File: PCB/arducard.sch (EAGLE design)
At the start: 85 parts, among them J1 USB MICRO, Q1 BC817-16LT1SMD, Q2 NTR0202PL, Q3 2N7002, Q4 BSS84, Q5 2N7002, Q6 2N7002, U1 microSD, U2 ATMEGA32U4-XUAU, U3 LM3658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

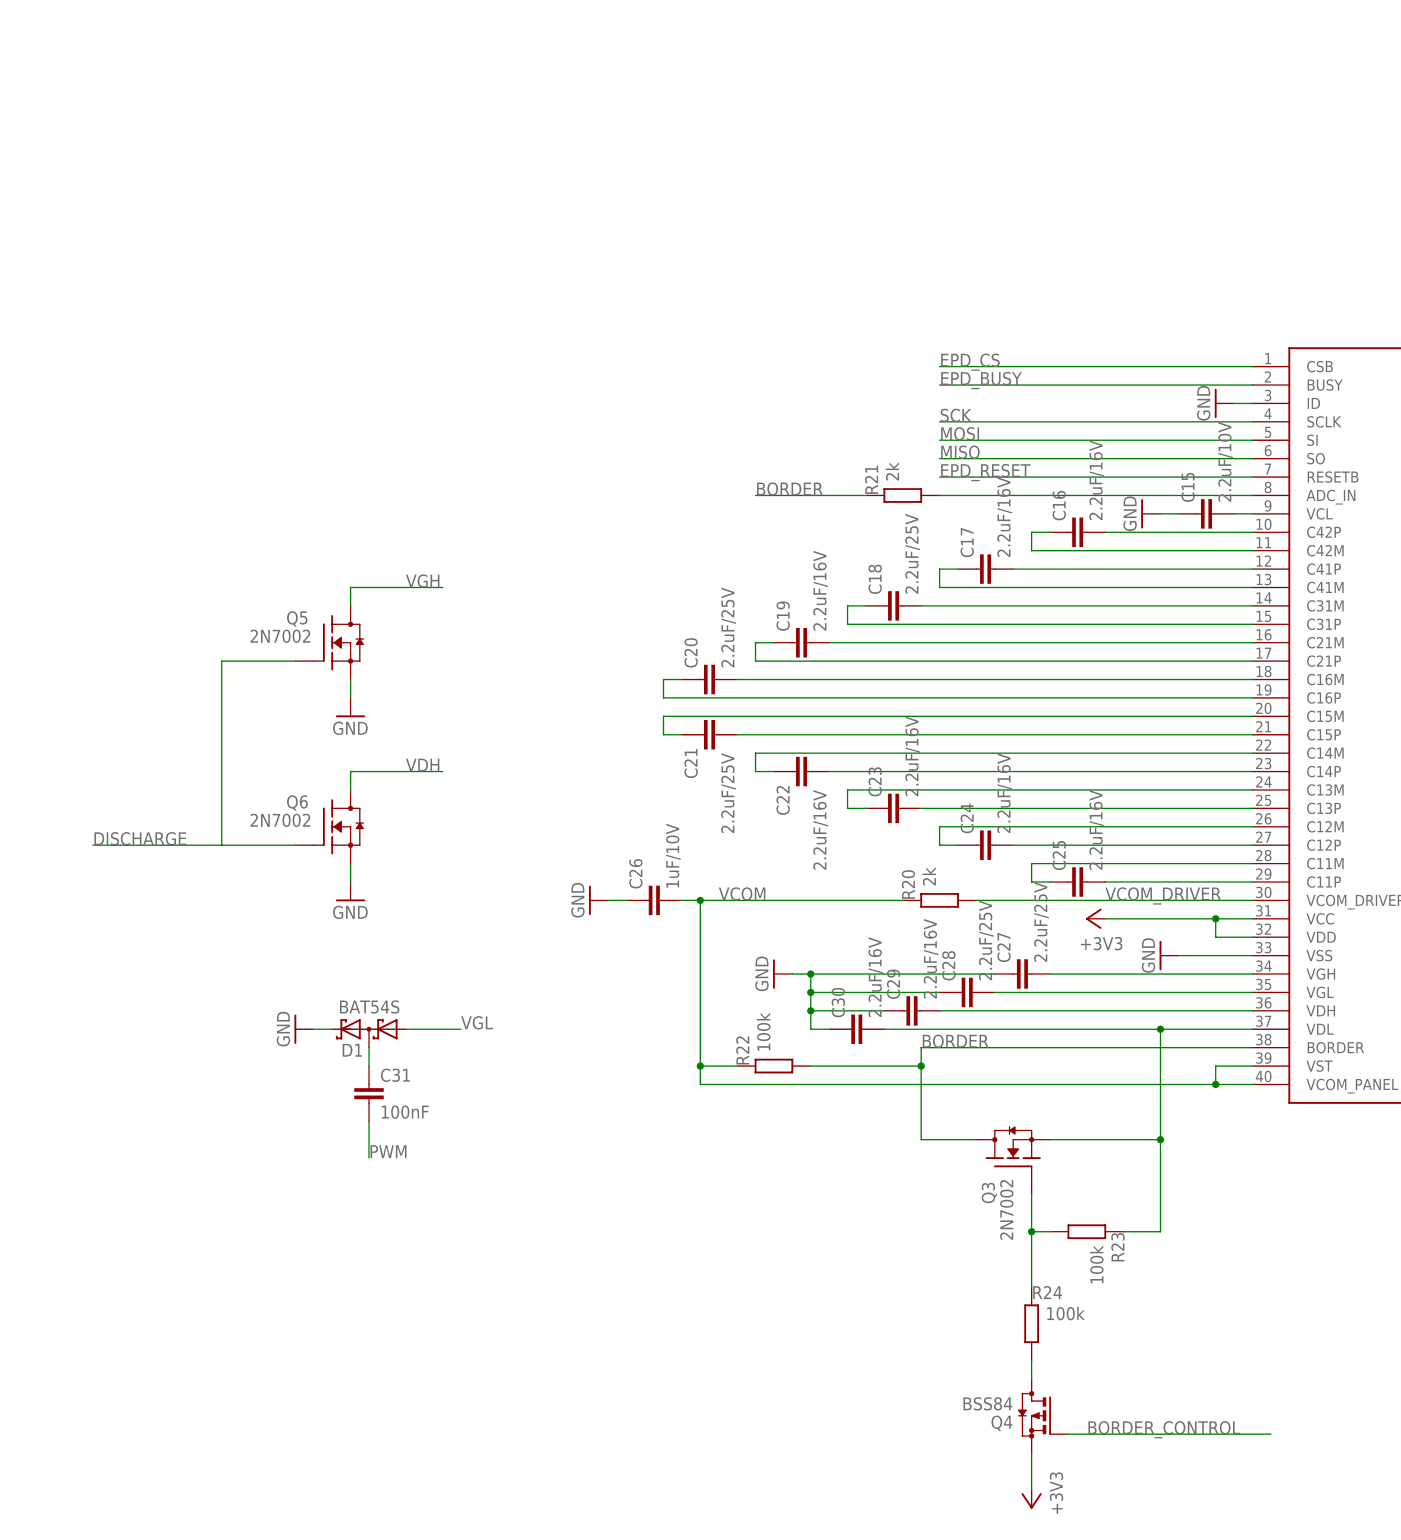
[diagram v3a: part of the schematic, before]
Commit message: Added EPD panel on control
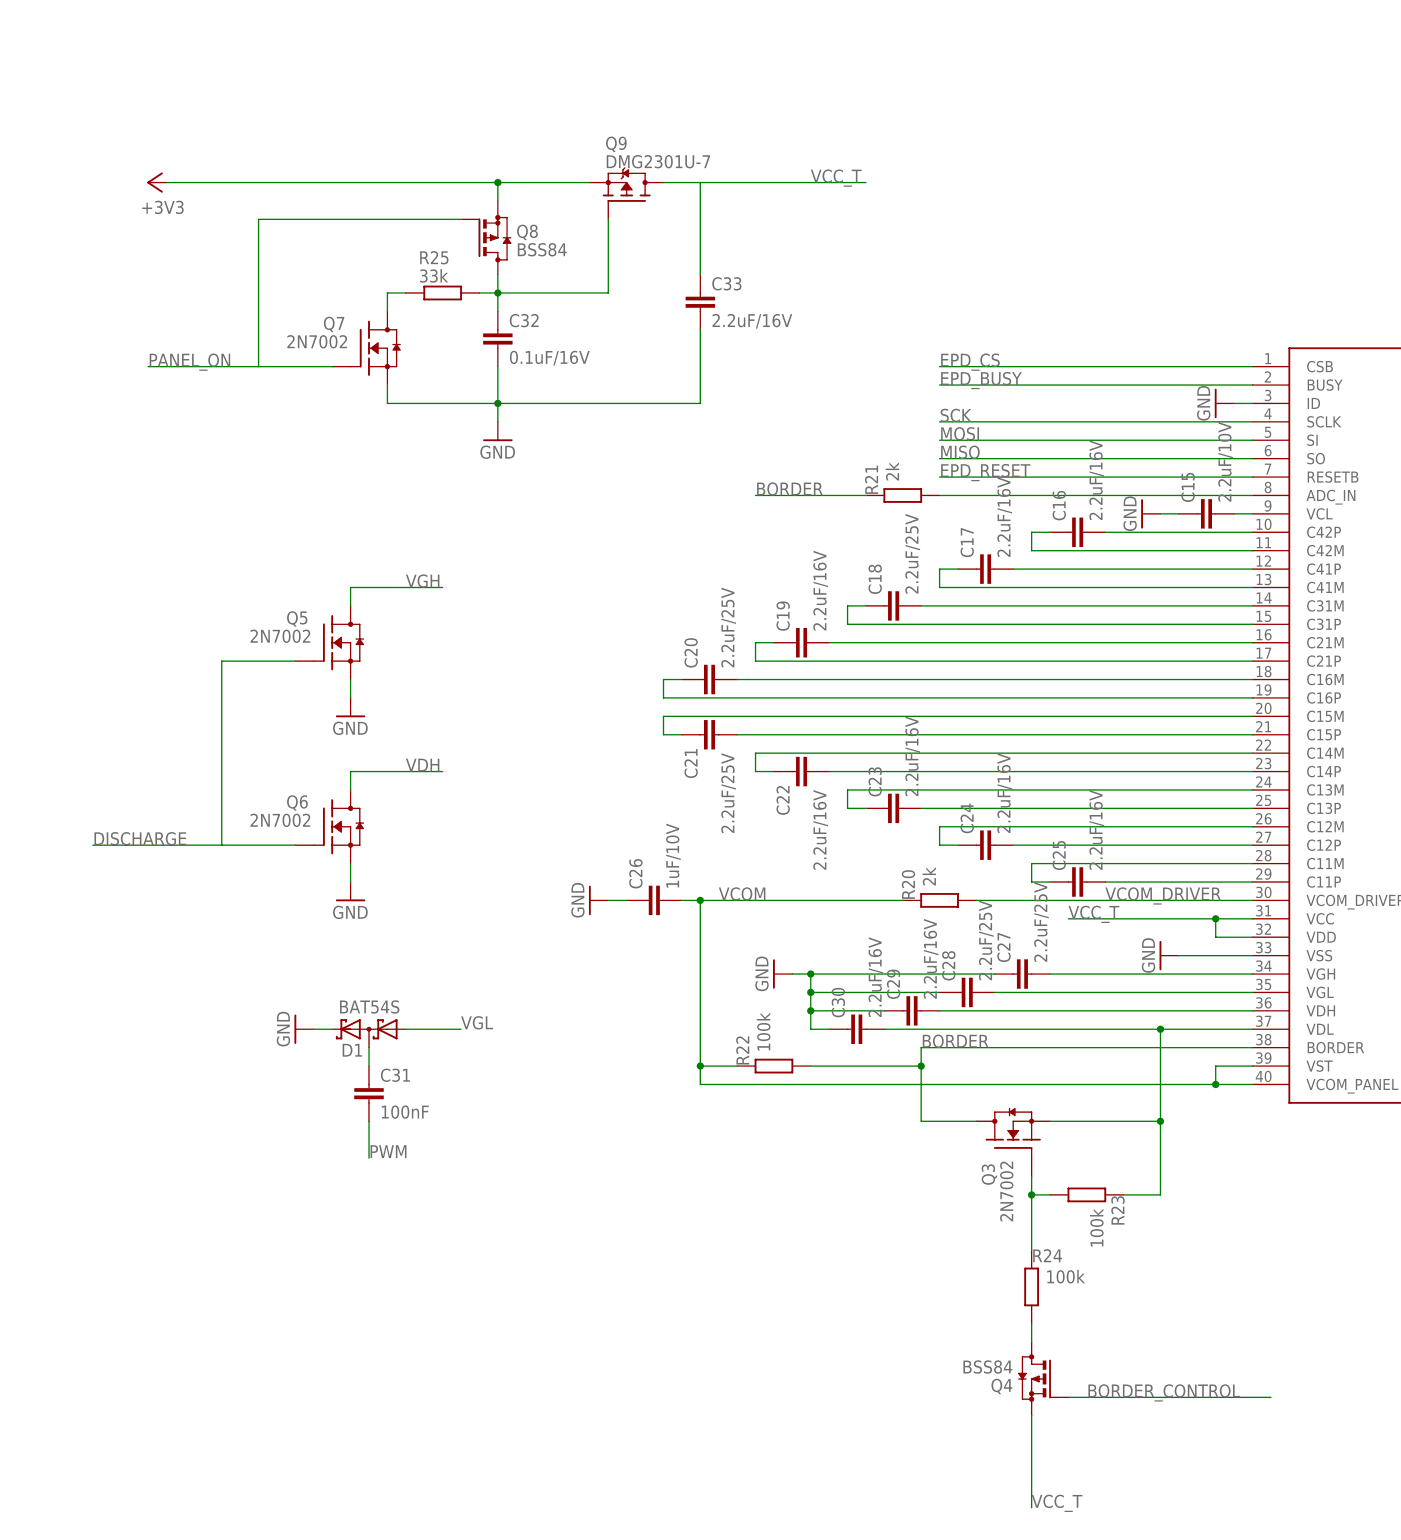
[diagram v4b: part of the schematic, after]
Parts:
- added C32: 0.1uF/16V, SmartPrj:C-EUC0603
- added C33: 2.2uF/16V, SmartPrj:C-EUC0603
- added Q7: 2N7002, AWJLEagleLib:2N7002
- added Q8: BSS84, transistor-small-signal:BSS84
- added Q9: DMG2301U-7, transistor-fet:DMG2301U-7
- added R25: 33k, SmartPrj:R-EU_R0603
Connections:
- new net N$34: Q7.D, R25.1
- new net N$44: C32.1, Q8.D, Q9.G, R25.2
- new net PANEL_ON: Q7.G, Q8.G
- new net VCC_T: C33.1, Q4.S, Q9.D, U$2.VCC, U$2.VDD
- net +3V3: now also Q8.S, Q9.S; no longer Q4.S, U$2.VCC, U$2.VDD
- net GND: now also C32.2, C33.2, Q7.S
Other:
- moved on the sheet: Q3, Q4, R23, R24

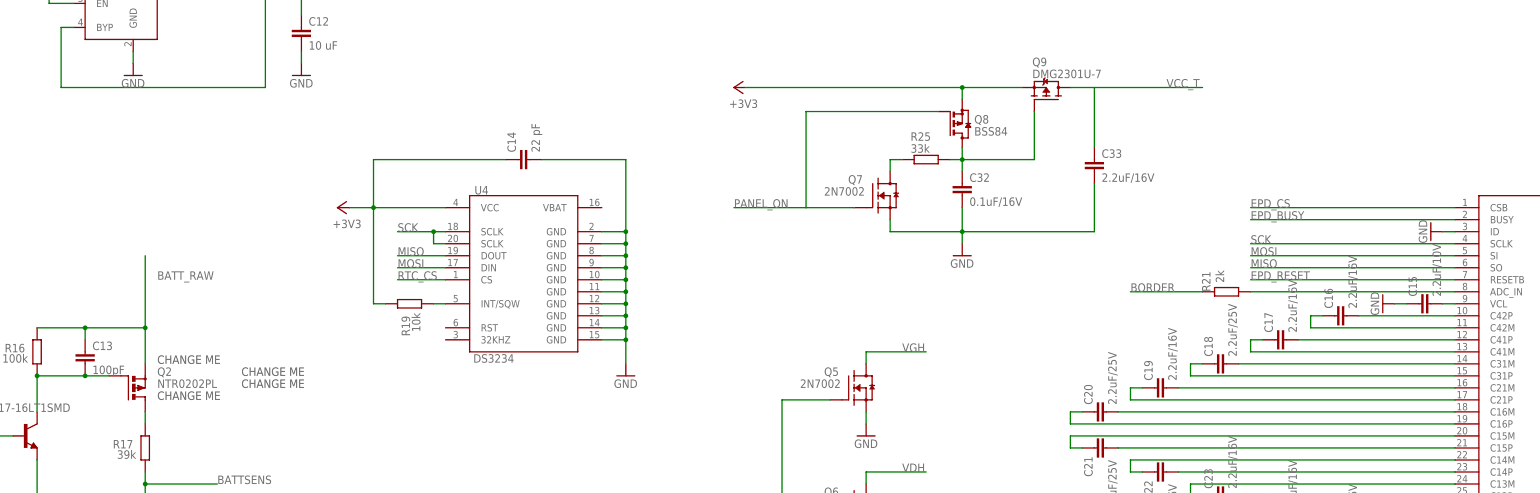
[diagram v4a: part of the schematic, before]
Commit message: Changed battery level sensing transistor
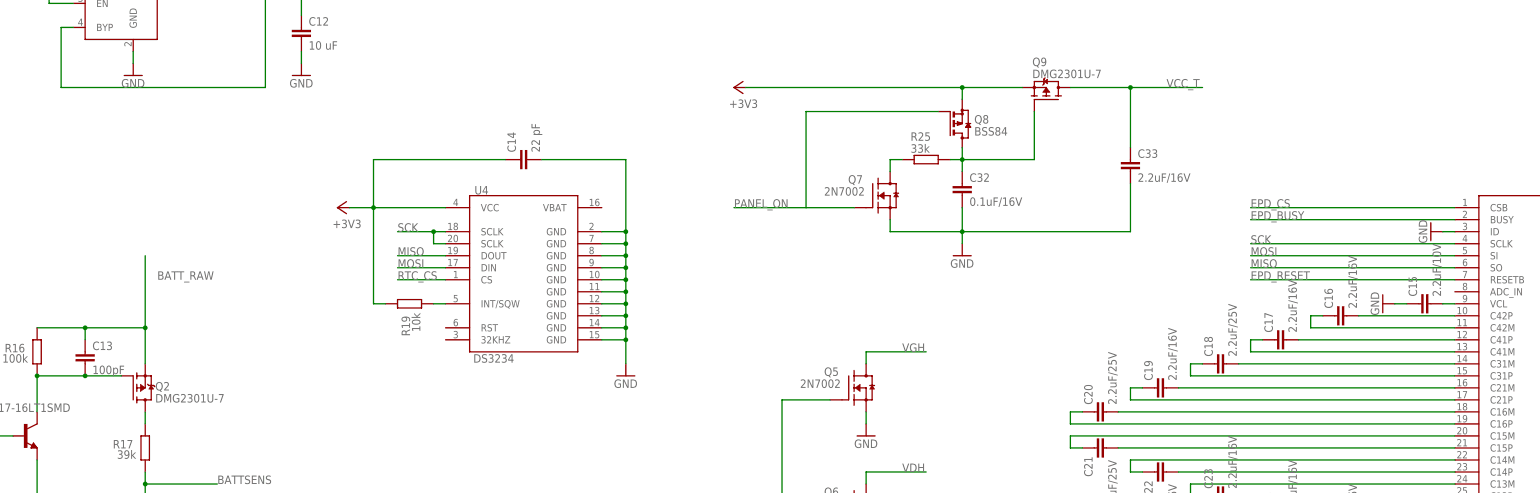
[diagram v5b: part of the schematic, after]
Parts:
- removed R21: 2k, SmartPrj:R-EU_R0603
- Q2: value NTR0202PL -> DMG2301U-7; device transistor-power:P-MOSFET-SO8 -> transistor-fet:DMG2301U-7
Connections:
- removed net N$41: R21.2, U$2.ADC_IN
- net BORDER: no longer R21.1
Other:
- note removed: "CHANGE ME"
- moved on the sheet: C33
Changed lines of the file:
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@@
 <part name="GND13" library="supply1" deviceset="GND" device=""/>
 <part name="Q1" library="transistor-npn" deviceset="BC817*" device="SMD" technology="-16LT1"/>
-<part name="Q2" library="transistor-power" deviceset="P-MOSFET-SO8" device="" value="NTR0202PL"/>
 <part name="R15" library="SmartPrj" deviceset="R-EU_" device="R0603" value="2k"/>
 <part name="R16" library="SmartPrj" deviceset="R-EU_" device="R0603" value="100k"/>
@@
 <part name="R20" library="SmartPrj" deviceset="R-EU_" device="R0603" value="2k"/>
 <part name="GND26" library="supply1" deviceset="GND" device=""/>
-<part name="R21" library="SmartPrj" deviceset="R-EU_" device="R0603" value="2k"/>
 <part name="R22" library="SmartPrj" deviceset="R-EU_" device="R0603" value="100k"/>
 <part name="R23" library="SmartPrj" deviceset="R-EU_" device="R0603" value="100k"/>
@@
 <part name="+3V11" library="supply1" deviceset="+3V3" device=""/>
 <part name="GND27" library="supply1" deviceset="GND" device=""/>
+<part name="Q2" library="transistor-fet" deviceset="DMG2301U-7" device="" value="DMG2301U-7"/>
 </parts>
 <sheets>
@@
 <plain>
 <text x="297.18" y="104.14" size="3.81" layer="94" ratio="10" rot="MR0">USB</text>
-<text x="548.64" y="35.56" size="1.778" layer="97">CHANGE ME</text>
-<text x="548.64" y="43.18" size="1.778" layer="97">CHANGE ME</text>
-<text x="566.42" y="40.64" size="1.778" layer="97">CHANGE ME</text>
-<text x="566.42" y="38.1" size="1.778" layer="97">CHANGE ME</text>
 </plain>
 <instances>
@@
 <instance part="GND13" gate="1" x="579.12" y="104.14"/>
 <instance part="Q1" gate="G$1" x="520.7" y="27.94"/>
-<instance part="Q2" gate="G$1" x="543.56" y="38.1"/>
 <instance part="R15" gate="G$1" x="508" y="27.94" smashed="yes">
 <attribute name="NAME" x="509.6764" y="30.48" size="1.778" layer="95" rot="R90"/>
@@
 </instance>
 <instance part="GND26" gate="1" x="731.52" y="2.54" rot="R270"/>
-<instance part="R21" gate="G$1" x="774.7" y="58.42" smashed="yes">
-<attribute name="NAME" x="771.2964" y="58.42" size="1.778" layer="95" rot="R90"/>
-<attribute name="VALUE" x="774.192" y="60.325" size="1.778" layer="96" rot="R90"/>
-</instance>
 <instance part="R22" gate="G$1" x="756.92" y="-20.32" smashed="yes">
 <attribute name="NAME" x="753.5164" y="-20.32" size="1.778" layer="95" rot="R90"/>
@@
 </instance>
 <instance part="C32" gate="G$1" x="718.82" y="81.28"/>
-<instance part="C33" gate="G$1" x="746.76" y="86.36"/>
+<instance part="C33" gate="G$1" x="754.38" y="86.36"/>
 <instance part="+3V11" gate="G$1" x="670.56" y="101.6" rot="R90"/>
 <instance part="GND27" gate="1" x="718.82" y="66.04"/>
+<instance part="Q2" gate="G$1" x="543.56" y="38.1" smashed="yes">
+<attribute name="VALUE" x="548.21" y="35.01" size="1.778" layer="96"/>
+<attribute name="NAME" x="548.21" y="37.55" size="1.778" layer="95"/>
+</instance>
 </instances>
 <busses>
@@
 <wire x1="718.82" y1="76.2" x2="718.82" y2="71.12" width="0.1524" layer="91"/>
 <pinref part="C33" gate="G$1" pin="2"/>
-<wire x1="718.82" y1="71.12" x2="746.76" y2="71.12" width="0.1524" layer="91"/>
-<wire x1="746.76" y1="71.12" x2="746.76" y2="81.28" width="0.1524" layer="91"/>
+<wire x1="718.82" y1="71.12" x2="754.38" y2="71.12" width="0.1524" layer="91"/>
+<wire x1="754.38" y1="71.12" x2="754.38" y2="81.28" width="0.1524" layer="91"/>
 <junction x="718.82" y="71.12"/>
 <pinref part="GND27" gate="1" pin="GND"/>
@@
 <pinref part="C13" gate="G$1" pin="1"/>
 <wire x1="533.4" y1="48.26" x2="533.4" y2="50.8" width="0.1524" layer="91"/>
-<pinref part="Q2" gate="G$1" pin="S"/>
 <wire x1="533.4" y1="50.8" x2="546.1" y2="50.8" width="0.1524" layer="91"/>
 <wire x1="546.1" y1="50.8" x2="546.1" y2="43.18" width="0.1524" layer="91"/>
@@
 <junction x="546.1" y="50.8"/>
 <label x="548.64" y="60.96" size="1.778" layer="95"/>
+<pinref part="Q2" gate="G$1" pin="S"/>
 </segment>
 </net>
@@
 <pinref part="Q1" gate="G$1" pin="C"/>
 <wire x1="523.24" y1="33.02" x2="523.24" y2="40.64" width="0.1524" layer="91"/>
-<pinref part="Q2" gate="G$1" pin="G"/>
-<wire x1="538.48" y1="40.64" x2="533.4" y2="40.64" width="0.1524" layer="91"/>
+<wire x1="541.02" y1="40.64" x2="533.4" y2="40.64" width="0.1524" layer="91"/>
 <pinref part="R16" gate="G$1" pin="1"/>
 <junction x="523.24" y="40.64"/>
@@
 <wire x1="533.4" y1="40.64" x2="523.24" y2="40.64" width="0.1524" layer="91"/>
 <junction x="533.4" y="40.64"/>
+<pinref part="Q2" gate="G$1" pin="G"/>
 </segment>
 </net>
 <net name="N$13" class="0">
 <segment>
-<pinref part="Q2" gate="G$1" pin="D"/>
 <pinref part="R17" gate="G$1" pin="2"/>
 <wire x1="546.1" y1="30.48" x2="546.1" y2="33.02" width="0.1524" layer="91"/>
+<pinref part="Q2" gate="G$1" pin="D"/>
 </segment>
 </net>
@@
 </segment>
 </net>
-<net name="N$41" class="0">
-<segment>
-<pinref part="U$2" gate="G$1" pin="ADC_IN"/>
-<wire x1="822.96" y1="58.42" x2="779.78" y2="58.42" width="0.1524" layer="91"/>
-<pinref part="R21" gate="G$1" pin="2"/>
-</segment>
-</net>
 <net name="BORDER" class="0">
-<segment>
-<pinref part="R21" gate="G$1" pin="1"/>
-<wire x1="769.62" y1="58.42" x2="754.38" y2="58.42" width="0.1524" layer="91"/>
-<label x="754.38" y="58.42" size="1.778" layer="95"/>
-</segment>
 <segment>
 <pinref part="U$2" gate="G$1" pin="BORDER"/>
@@
 <segment>
 <pinref part="C33" gate="G$1" pin="1"/>
-<wire x1="746.76" y1="88.9" x2="746.76" y2="101.6" width="0.1524" layer="91"/>
+<wire x1="754.38" y1="88.9" x2="754.38" y2="101.6" width="0.1524" layer="91"/>
 <pinref part="Q9" gate="G$1" pin="D"/>
-<wire x1="741.68" y1="101.6" x2="746.76" y2="101.6" width="0.1524" layer="91"/>
-<wire x1="746.76" y1="101.6" x2="769.62" y2="101.6" width="0.1524" layer="91"/>
+<wire x1="741.68" y1="101.6" x2="754.38" y2="101.6" width="0.1524" layer="91"/>
+<wire x1="754.38" y1="101.6" x2="769.62" y2="101.6" width="0.1524" layer="91"/>
 <label x="762" y="101.6" size="1.778" layer="95"/>
-</segment>
-<segment>
+<junction x="754.38" y="101.6"/>
+</segment>
+<segment>

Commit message: added battery connector
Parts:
- removed C10: 1uF, SmartPrj:C-EUC0603
- removed R14, R3: NM, SmartPrj:R-EU_R0402
- removed R4: 10k, ptc-ntc:NTC640-9
- removed U3: LM3658, national-semiconductor:LM3658
- added R21: 18.2k, SmartPrj:R-EU_R0603
- added U$3: XC6802A42XMR-G, arducard-xc6802:XC6802A42XMR-G
- added U$4: PGEB016144, arducard-battery:PGEB016144
- JP1: value (none) -> M02PTH; device pinhead:PINHD-1X2 -> SparkFun-Connectors:M02PTH
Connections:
- removed net N$8: C6.2, R14.1
- removed net UGND: C7.2, J1.GND, L2.1, R3.2, U2.UGND
- new net N$37: R21.2, U$3.ISEN
- net BATTSTAT1: no longer U3.STAT1
- net BATTSTAT2: no longer U3.STAT2
- net BATT_RAW: now also U$3.BAT, U$4.+; no longer C10.1, U3.BATT
- net GND: now also C6.2, C7.2, J1.GND, L2.1, R21.1, U$3.VSS, U$4.-, U2.UGND; no longer C10.2, R14.2, R3.1, R4.2, U3.EN_B, U3.GND, U3.GND_PAD
- net N$4: now also U$3./CHG; no longer R4.1, U3.TS
- net VUSB: now also U$3.VIN; no longer U3.USB_PWR, U3.USB_SEL
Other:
- moved on the sheet: C5, JP1
